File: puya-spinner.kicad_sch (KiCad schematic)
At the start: 50 parts, among them J1 Conn_ARM_SWD_TagConnect_TC2030, U1 PY32F002AF15P6, U2 SC7A20

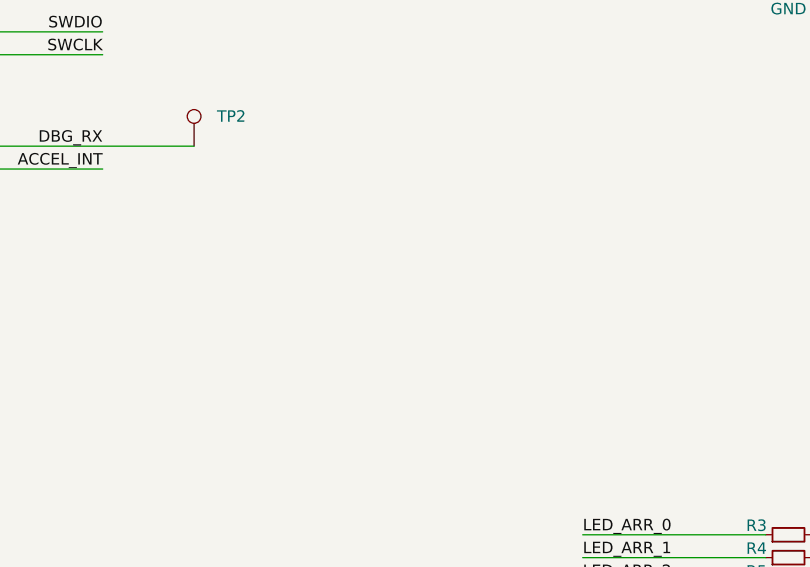
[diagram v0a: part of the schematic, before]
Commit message: FIXME add bearing
need to change tolerances
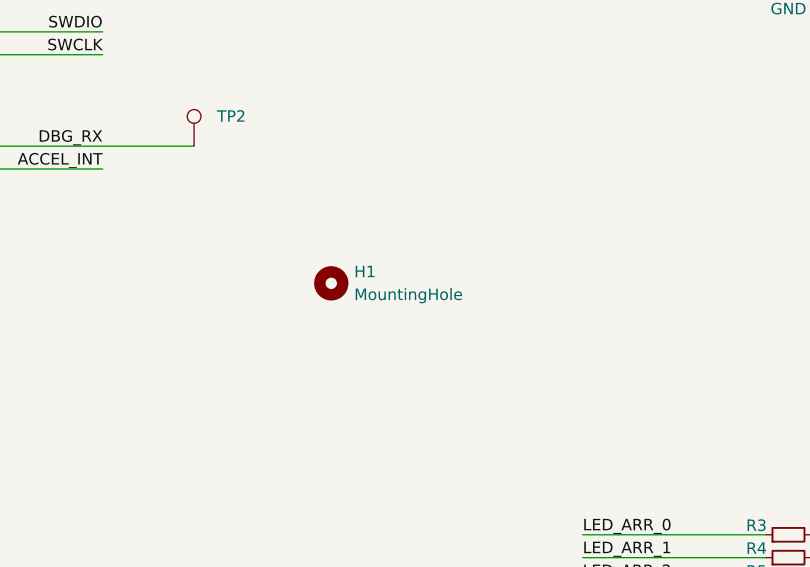
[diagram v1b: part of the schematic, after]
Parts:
- added H1: MountingHole, parts:fixme_608_bearing, symbol Mechanical:MountingHole
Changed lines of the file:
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@@
+	)
+	(symbol
+		(lib_id "Mechanical:MountingHole")
+		(at 127 76.2 0)
+		(unit 1)
+		(exclude_from_sim yes)
+		(in_bom no)
+		(on_board yes)
+		(dnp no)
+		(fields_autoplaced yes)
+		(property "Reference" "H1"
+			(at 129.54 74.9299 0)
+			(effects
+				(font
+					(size 1.27 1.27)
+				)
+				(justify left)
+			)
+		)
+		(property "Value" "MountingHole"
+			(at 129.54 77.4699 0)
+			(effects
+				(font
+					(size 1.27 1.27)
+				)
+				(justify left)
+			)
+		)
+		(property "Footprint" "parts:fixme_608_bearing"
+			(at 127 76.2 0)
+			(effects
+				(font
+					(size 1.27 1.27)
+				)
+				(hide yes)
+			)
+		)
+		(property "Datasheet" "~"
+			(at 127 76.2 0)
+			(effects
+				(font
+					(size 1.27 1.27)
+				)
+				(hide yes)
+			)
+		)
+		(property "Description" "Mounting Hole without connection"
+			(at 127 76.2 0)
+			(effects
+				(font
+					(size 1.27 1.27)
+				)
+				(hide yes)
+			)
+		)
+		(instances
+			(project "puya-spinner"
+				(path "/55924447-94dd-4524-a9d3-3f79a9e023c8"
+					(reference "H1")
+					(unit 1)
+				)
+			)
+		)
 	)
 	(symbol

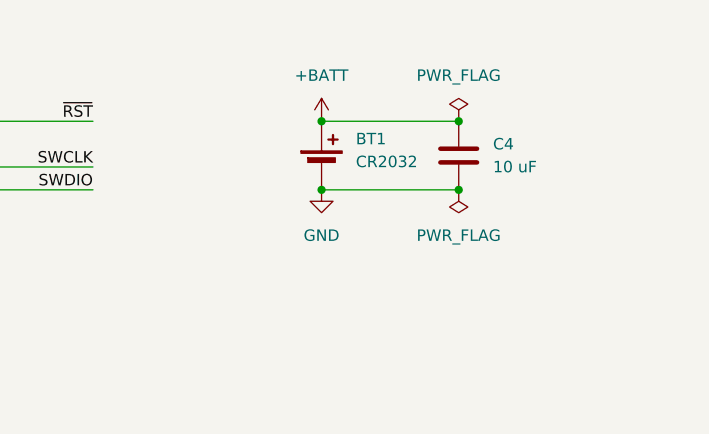
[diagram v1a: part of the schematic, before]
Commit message: fix bearing hole; add reverse polarity protection
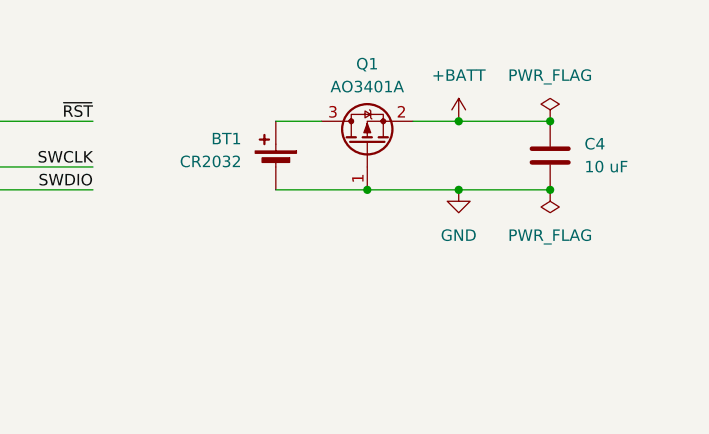
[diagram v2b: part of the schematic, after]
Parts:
- added Q1: AO3401A, Package_TO_SOT_SMD:SOT-23, symbol Transistor_FET:AO3401A
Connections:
- net +BATT: now also Q1.2 (S); no longer BT1.1 (+)
- net GND: now also Q1.1 (G)
- new net: BT1.1 (+), Q1.3 (D)
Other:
- moved on the sheet: BT1, C4

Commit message: revA for fab
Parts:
- BT1: LCSC (none) -> C2979167
- H1: value MountingHole -> 608 bearing
- TP1, TP2: now left out of the parts list
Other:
- company: (none) -> ArcaneNibble
- title: (none) -> PY32 POV spinner demo
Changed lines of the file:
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@@
 	(generator_version "8.0")
 	(paper "A4")
+	(title_block
+		(title "PY32 POV spinner demo")
+		(date "2024-08-18")
+		(rev "A")
+		(company "ArcaneNibble")
+	)
 	(junction
 		(at 228.6 116.84)
@@
 			)
 		)
+		(property "LCSC" "C2979167"
+			(at 223.52 30.48 0)
+			(effects
+				(font
+					(size 1.27 1.27)
+				)
+				(hide yes)
+			)
+		)
 		(pin "1"
 		)
@@
 			)
 		)
-		(property "Value" "MountingHole"
+		(property "Value" "608 bearing"
 			(at 129.54 77.4699 0)
 			(effects
@@
 		(unit 1)
 		(exclude_from_sim no)
-		(in_bom yes)
+		(in_bom no)
 		(on_board yes)
 		(dnp no)
@@
 		(unit 1)
 		(exclude_from_sim no)
-		(in_bom yes)
+		(in_bom no)
 		(on_board yes)
 		(dnp no)
